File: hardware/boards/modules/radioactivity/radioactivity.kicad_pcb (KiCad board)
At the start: 2 copper layers, 95 x 75 mm, 56 parts, among them J1 jmp1, J2 Programming Header, J3 jmp1, Q1 S8050, Q2 MMBTA42, Q3 S8050, Q4 S8050, T1 74LVC1G17GW, U1 TLC555, U2 TLC555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

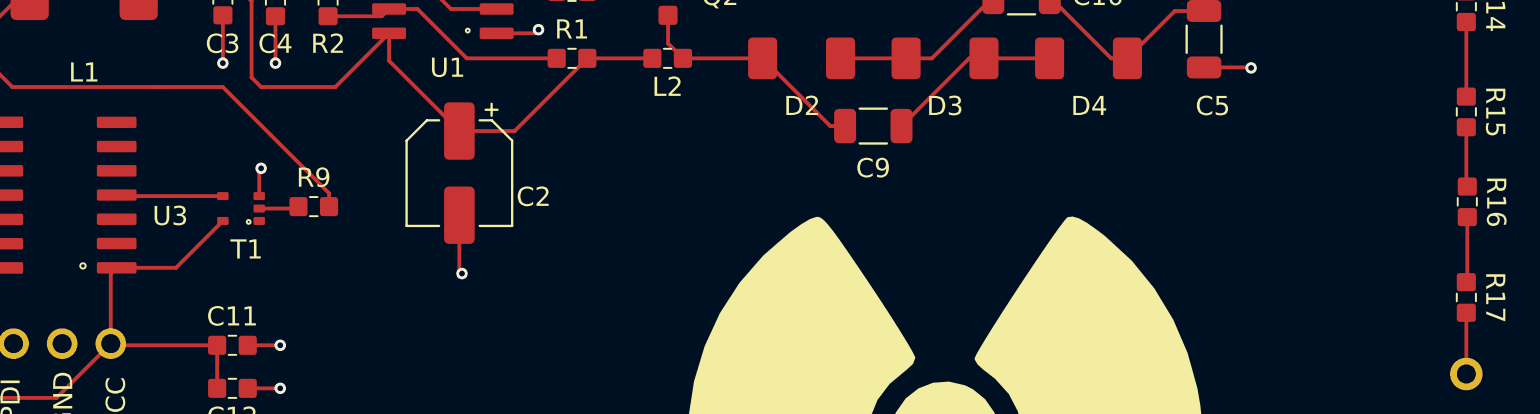
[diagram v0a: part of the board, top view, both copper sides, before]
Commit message: added missing status LED to radioactivity board
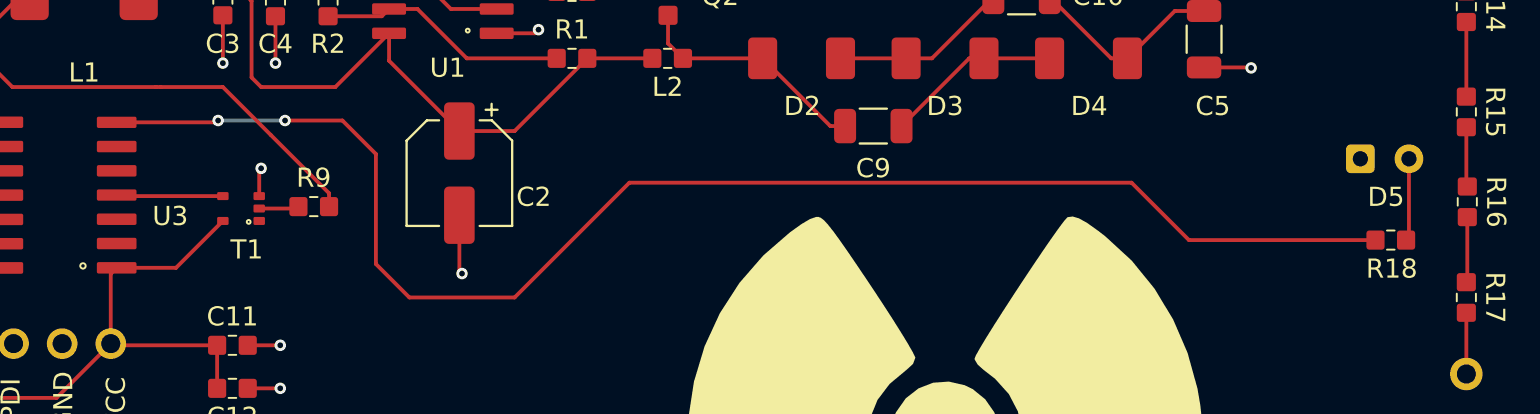
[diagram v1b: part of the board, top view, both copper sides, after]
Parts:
- added D5: ~, common:LED_3mm_THT, F.Cu at (179.6, 106.5)
- added R18: 220, common:R_0603, F.Cu at (179.8, 107.8)
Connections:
- U3 pad 7: unconnected-(U3-TOSC2/PB2-Pad7) -> STATUS_LED
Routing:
- net STATUS_LED: track 0.00 -> 76.8 mm, vias 0 -> 2
- net Net-(D5-A): track 0.00 -> 4.31 mm

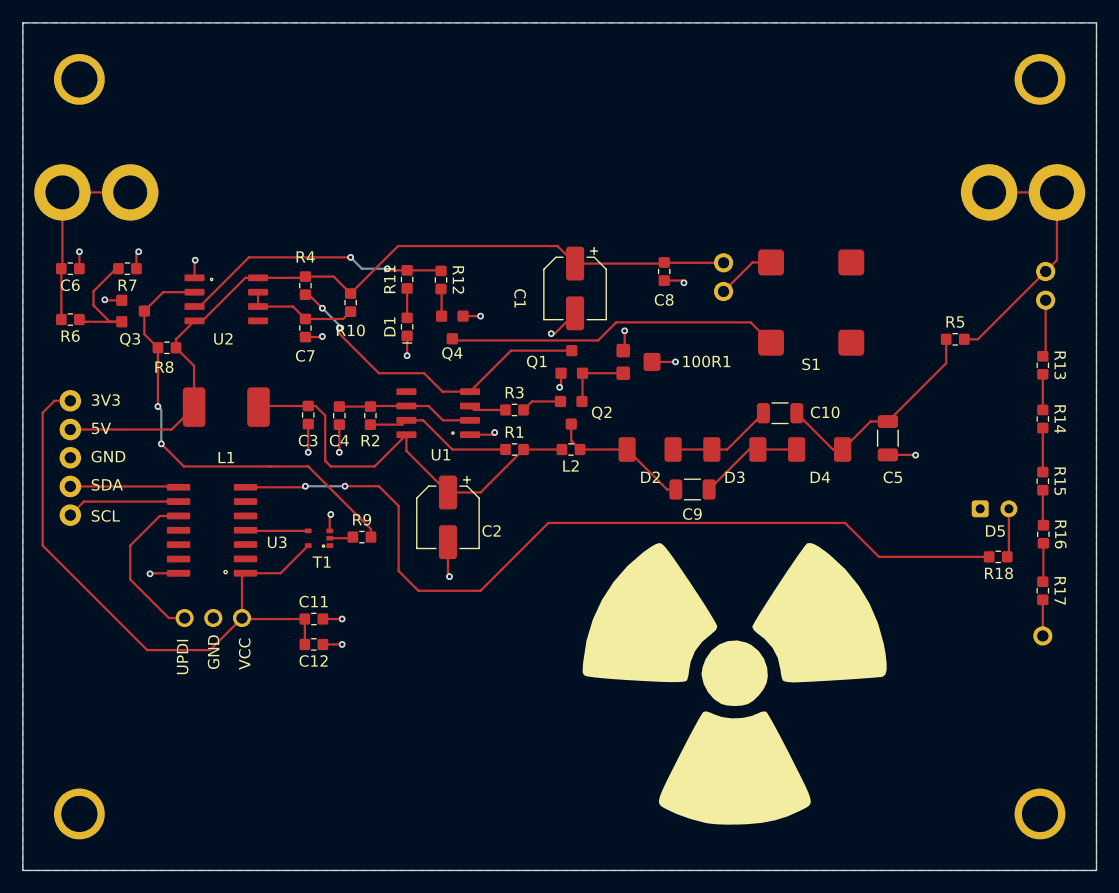
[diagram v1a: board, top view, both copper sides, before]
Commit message: updated sensor module schematics
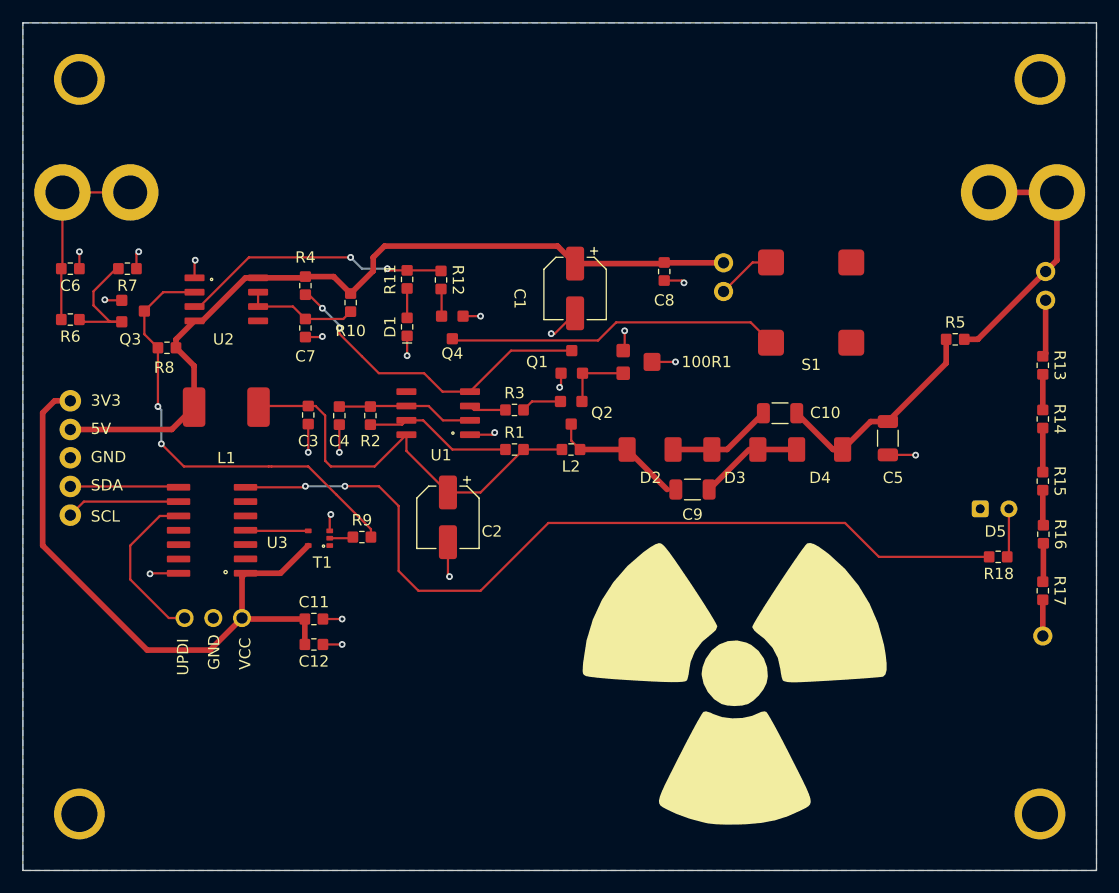
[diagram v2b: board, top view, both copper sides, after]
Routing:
- net 5V: track 72.2 -> 72.9 mm
